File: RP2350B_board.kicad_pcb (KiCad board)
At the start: 2 copper layers, 47.5 x 66 mm, 45 parts, among them IC1 W25Q128JVSIM, IC2 UA78M33CDCYG3, J1 USB_C_Receptacle_USB2.0_16P, J2 SWD, J3 Conn_01x25_Pin, J4 Conn_01x25_Pin, J5 Conn_01x25_Pin, J6 Conn_01x25_Pin, J7 Conn_01x25_Pin, J8 Conn_01x25_Pin, U1 RP2350_80QFN, Y1 ABM8-272-T3

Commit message: refactor: start new layout
Signed-off-by: Aditya Agarwal <aditya.agarwal030504@gmail.com>
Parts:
- removed G***: LOGO, Dumblebots-Logo:Dumblebots-Logo
- removed IC2: UA78M33CDCYG3, UA78M33CDCYG3:SOT230P700X180-4N
- removed R5: 0, Resistor_SMD:R_0402_1005Metric
- removed R8: 1K, Resistor_SMD:R_0402_1005Metric
- added R10: 27, Resistor_SMD:R_0402_1005Metric, F.Cu at (237.2, 104.0)
- added R11: 27, Resistor_SMD:R_0402_1005Metric, F.Cu at (236.2, 104.0)
- added U2: NCP1117-3.3_SOT223, Package_TO_SOT_SMD:SOT-223-3_TabPin2, F.Cu at (242.6, 90.8)
- C19, C20: value 100n -> 10u
- J2: value SWD -> MEM2080-00-128-00-A; footprint Connector_PinHeader_2.54mm:PinHeader_1x04_P2.54mm_Vertical -> MEM2080-00-128-00-A:MEM20800012800A
- L1: footprint Inductor_SMD:L_0603_1608Metric -> Inductor_SMD:L_0805_2012Metric
- R4: value 10K -> 1K
- R6: value DNF -> 10K
- moved R4 122.1 mm to (243.3, 143.4), turned to -90 degrees
- moved C13 108.2 mm to (243.3, 114.0), turned to 0 degrees
- moved C12 104.4 mm to (243.3, 117.7), turned to 0 degrees
- moved C14 104.1 mm to (234.8, 121.8), turned to -90 degrees
- moved C6 102.1 mm to (239.5, 106.2), turned to 0 degrees
- moved C16 99.8 mm to (232.3, 120.9), turned to 180 degrees
- moved C11 99.0 mm to (239.5, 107.2), turned to 0 degrees
- moved R6 97.5 mm to (227.7, 104.7), turned to -45 degrees
- moved C3 95.2 mm to (241.8, 108.4), turned to -90 degrees
- moved S2 95.1 mm to (230.0, 89.7), turned to 90 degrees
- moved C18 94.7 mm to (238.3, 126.5), turned to -90 degrees
- moved R9 94.4 mm to (228.5, 103.9), turned to -45 degrees
- moved C15 92.6 mm to (227.0, 110.7), turned to 180 degrees
- moved R7 92.3 mm to (237.3, 126.5)
- moved L1 92.1 mm to (239.6, 104.6)
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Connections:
- net /VREG_LX renamed VREG_LX
- net Net-(U1-XOUT) renamed XOUT
- C1 pad 1: /VREG_AVDD -> IOVDD
- C1 pad 2: GND -> VREG_PGND
- C10 pad 1: +3.3v -> IOVDD
- C10 pad 2: GND -> VREG_PGND
- C11 pad 1: +3.3v -> IOVDD
- C11 pad 2: GND -> VREG_PGND
- C12 pad 1: +3.3v -> IOVDD
- C12 pad 2: GND -> VREG_PGND
- C13 pad 1: +3.3v -> IOVDD
- C13 pad 2: GND -> VREG_PGND
- C14 pad 1: +3.3v -> IOVDD
- C14 pad 2: GND -> VREG_PGND
- C15 pad 1: +3.3v -> IOVDD
- C15 pad 2: GND -> VREG_PGND
- C16 pad 1: +3.3v -> IOVDD
- C16 pad 2: GND -> VREG_PGND
- C17 pad 1: Net-(U1-XIN) -> VREG_PGND
- C17 pad 2: GND -> XIN
- C18 pad 1: Net-(Y1-CRYSTAL_2) -> VREG_PGND
- C18 pad 2: GND -> Net-(C18-Pad2)
- C19 pad 2: GND -> VREG_PGND
- C2 pad 1: +3.3v -> DVDD
- C2 pad 2: GND -> VREG_PGND
- C20 pad 1: GND -> IOVDD
- C20 pad 2: +3.3v -> VREG_PGND
- C3 pad 1: +1V1 -> VREG_AVDD
- C3 pad 2: GND -> VREG_PGND
- C4 pad 1: +1V1 -> DVDD
- C4 pad 2: GND -> VREG_PGND
- C5 pad 1: +1V1 -> DVDD
- C5 pad 2: GND -> VREG_PGND
- C6 pad 1: +1V1 -> DVDD
- C6 pad 2: GND -> VREG_PGND
- C7 pad 1: +3.3v -> IOVDD
- C7 pad 2: GND -> VREG_PGND
- C8 pad 1: +3.3v -> IOVDD
- C8 pad 2: GND -> VREG_PGND
- C9 pad 1: +3.3v -> IOVDD
- C9 pad 2: GND -> VREG_PGND
- IC1 pad 1: Net-(IC1-~{CS}) -> GPIO0
- IC1 pad 4: GND -> VREG_PGND
- IC1 pad 8: +3.3v -> IOVDD
- J1 pad A1: GND -> VREG_PGND
- J1 pad A12: GND -> VREG_PGND
- J1 pad A6: USB_D+ -> Net-(J1-D+-PadA6)
- J1 pad A7: USB_D- -> Net-(J1-D--PadA7)
- J1 pad B1: GND -> VREG_PGND
- J1 pad B12: GND -> VREG_PGND
- J1 pad B6: USB_D+ -> Net-(J1-D+-PadA6)
- J1 pad B7: USB_D- -> Net-(J1-D--PadA7)
- J1 pad S1: GND -> VREG_PGND
- J2 pad 1: +3.3v -> unconnected-(J2-DAT2-Pad1)
- J2 pad 2: SWD -> unconnected-(J2-CD/DAT3-Pad2)
- J2 pad 3: SWCLK -> unconnected-(J2-CMD-Pad3)
- J2 pad 4: GND -> unconnected-(J2-VDD-Pad4)
- J4 pad 10: GND -> VREG_PGND
- J5 pad 1: GND -> VREG_PGND
- J5 pad 10: GND -> VREG_PGND
- J5 pad 11: GND -> VREG_PGND
- J5 pad 12: GND -> VREG_PGND
- J5 pad 13: GND -> VREG_PGND
- J5 pad 14: GND -> VREG_PGND
- J5 pad 15: GND -> VREG_PGND
- J5 pad 16: GND -> VREG_PGND
- J5 pad 17: GND -> VREG_PGND
- J5 pad 18: GND -> VREG_PGND
- J5 pad 19: GND -> VREG_PGND
- J5 pad 2: GND -> VREG_PGND
- J5 pad 20: GND -> VREG_PGND
- J5 pad 21: GND -> VREG_PGND
- J5 pad 22: GND -> VREG_PGND
- J5 pad 23: GND -> VREG_PGND
- J5 pad 24: GND -> VREG_PGND
- J5 pad 25: GND -> VREG_PGND
- J5 pad 3: GND -> VREG_PGND
- J5 pad 4: GND -> VREG_PGND
- J5 pad 5: GND -> VREG_PGND
- J5 pad 6: GND -> VREG_PGND
- J5 pad 7: GND -> VREG_PGND
- J5 pad 8: GND -> VREG_PGND
- J5 pad 9: GND -> VREG_PGND
- J6 pad 1: GND -> VREG_PGND
- J6 pad 10: GND -> VREG_PGND
- J6 pad 11: GND -> VREG_PGND
- J6 pad 12: GND -> VREG_PGND
- J6 pad 13: GND -> VREG_PGND
- J6 pad 14: GND -> VREG_PGND
- J6 pad 15: GND -> VREG_PGND
- J6 pad 16: GND -> VREG_PGND
- J6 pad 17: GND -> VREG_PGND
- J6 pad 18: GND -> VREG_PGND
- J6 pad 19: GND -> VREG_PGND
- J6 pad 2: GND -> VREG_PGND
- J6 pad 20: GND -> VREG_PGND
- J6 pad 21: GND -> VREG_PGND
- J6 pad 22: GND -> VREG_PGND
- J6 pad 23: GND -> VREG_PGND
- J6 pad 24: GND -> VREG_PGND
- J6 pad 25: GND -> VREG_PGND
- J6 pad 3: GND -> VREG_PGND
- J6 pad 4: GND -> VREG_PGND
- J6 pad 5: GND -> VREG_PGND
- J6 pad 6: GND -> VREG_PGND
- J6 pad 7: GND -> VREG_PGND
- J6 pad 8: GND -> VREG_PGND
- J6 pad 9: GND -> VREG_PGND
- J7 pad 1: +3.3v -> IOVDD
- J7 pad 10: +3.3v -> IOVDD
- J7 pad 11: +3.3v -> IOVDD
- J7 pad 12: +3.3v -> IOVDD
- J7 pad 13: +3.3v -> IOVDD
- J7 pad 14: +3.3v -> IOVDD
- J7 pad 15: +3.3v -> IOVDD
- J7 pad 16: +3.3v -> IOVDD
- J7 pad 17: +3.3v -> IOVDD
- J7 pad 18: +3.3v -> IOVDD
- J7 pad 19: +3.3v -> IOVDD
- J7 pad 2: +3.3v -> IOVDD
- J7 pad 20: +3.3v -> IOVDD
- J7 pad 21: +3.3v -> IOVDD
- J7 pad 22: +3.3v -> IOVDD
- J7 pad 23: +3.3v -> IOVDD
- J7 pad 24: +3.3v -> IOVDD
- J7 pad 25: +3.3v -> IOVDD
- J7 pad 3: +3.3v -> IOVDD
- J7 pad 4: +3.3v -> IOVDD
- J7 pad 5: +3.3v -> IOVDD
- J7 pad 6: +3.3v -> IOVDD
- J7 pad 7: +3.3v -> IOVDD
- J7 pad 8: +3.3v -> IOVDD
- J7 pad 9: +3.3v -> IOVDD
- J8 pad 1: +3.3v -> IOVDD
- J8 pad 10: +3.3v -> IOVDD
- J8 pad 11: +3.3v -> IOVDD
- J8 pad 12: +3.3v -> IOVDD
- J8 pad 13: +3.3v -> IOVDD
- J8 pad 14: +3.3v -> IOVDD
- J8 pad 15: +3.3v -> IOVDD
- J8 pad 16: +3.3v -> IOVDD
- J8 pad 17: +3.3v -> IOVDD
- J8 pad 18: +3.3v -> IOVDD
- J8 pad 19: +3.3v -> IOVDD
- J8 pad 2: +3.3v -> IOVDD
- J8 pad 20: +3.3v -> IOVDD
- J8 pad 21: +3.3v -> IOVDD
- J8 pad 22: +3.3v -> IOVDD
- J8 pad 23: +3.3v -> IOVDD
- J8 pad 24: +3.3v -> IOVDD
- J8 pad 25: +3.3v -> IOVDD
- J8 pad 3: +3.3v -> IOVDD
- J8 pad 4: +3.3v -> IOVDD
- J8 pad 5: +3.3v -> IOVDD
- J8 pad 6: +3.3v -> IOVDD
- J8 pad 7: +3.3v -> IOVDD
- J8 pad 8: +3.3v -> IOVDD
- J8 pad 9: +3.3v -> IOVDD
- L1 pad 1: +1V1 -> DVDD
- R1 pad 1: +3.3v -> IOVDD
- R1 pad 2: /VREG_AVDD -> VREG_AVDD
- R2 pad 2: GND -> VREG_PGND
- R3 pad 2: GND -> VREG_PGND
- R4 pad 1: Net-(IC1-~{CS}) -> VREG_PGND
- R4 pad 2: +3.3v -> Net-(S1-NO)
- R6 pad 2: Net-(IC1-~{CS}) -> IOVDD
- R7 pad 1: Net-(Y1-CRYSTAL_2) -> Net-(C18-Pad2)
- R9 pad 1: GND -> GPIO0
- R9 pad 2: Net-(S2-NO) -> Net-(S2-COM)
- S2 pad 1: QSPI_SS -> Net-(S2-COM)
- S2 pad 2: Net-(S2-NO) -> VREG_PGND
- U1 pad 10: +1V1 -> DVDD
- U1 pad 15: +3.3v -> IOVDD
- U1 pad 24: +3.3v -> IOVDD
- U1 pad 29: +3.3v -> IOVDD
- U1 pad 30: Net-(U1-XIN) -> XIN
- U1 pad 32: +1V1 -> DVDD
- U1 pad 41: +3.3v -> IOVDD
- U1 pad 5: +3.3v -> IOVDD
- U1 pad 50: +3.3v -> IOVDD
- U1 pad 51: +1V1 -> DVDD
- U1 pad 59: +3.3v -> IOVDD
- U1 pad 60: +3.3v -> IOVDD
- U1 pad 61: /VREG_AVDD -> VREG_AVDD
- U1 pad 62: GND -> VREG_PGND
- U1 pad 64: +3.3v -> IOVDD
- U1 pad 65: +1V1 -> DVDD
- U1 pad 68: +3.3v -> IOVDD
- U1 pad 69: +3.3v -> IOVDD
- U1 pad 75: QSPI_SS -> GPIO0
- U1 pad 76: +3.3v -> IOVDD
- U1 pad 81: GND -> VREG_PGND
- Y1 pad 1: Net-(U1-XIN) -> XIN
- Y1 pad 2: GND -> VREG_PGND
- Y1 pad 3: Net-(Y1-CRYSTAL_2) -> Net-(C18-Pad2)
- Y1 pad 4: GND -> VREG_PGND
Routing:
- net +3.3v: track 421.7 -> 0.00 mm, vias 16 -> 0
- net QSPI_SS: track 50.9 -> 0.00 mm, vias 1 -> 0
- net IOVDD: track 0.00 -> 48.8 mm, vias 0 -> 2
- net GND: track 37.4 -> 0.00 mm, vias 27 -> 0
- net GPIO47: track 33.0 -> 0.00 mm
- net GPIO25: track 32.1 -> 0.00 mm, vias 2 -> 0
- net GPIO46: track 31.9 -> 0.00 mm
- net GPIO45: track 30.8 -> 0.00 mm
- net GPIO1: track 30.5 -> 0.00 mm
- net GPIO26: track 30.3 -> 0.00 mm, vias 2 -> 0
- net GPIO24: track 29.5 -> 0.00 mm
- net GPIO2: track 27.8 -> 0.00 mm
- net GPIO27: track 26.8 -> 0.00 mm, vias 2 -> 0
- net GPIO23: track 26.6 -> 0.00 mm
- net GPIO44: track 25.6 -> 0.00 mm
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- removed copper zone on B.Cu, net GND
- removed copper zone on F.Cu, net GND
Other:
- board size 47.5 x 66 mm -> 43 x 79 mm
- board text removed: "05"
- board text removed: "06"
- board text removed: "12"
- board text removed: "3V3"
- board text removed: "42"
- board text removed: "43"
- board text removed: "44"
- board text removed: "BOOT"
- board text removed: "Designed and manufactured in Bharat"
- board text removed: "GND"
- board text removed: "GPIO01"
- board text removed: "GPIO02"
- board text removed: "GPIO03"
- board text removed: "GPIO04"
- board text removed: "GPIO07"
- board text removed: "GPIO08"
- board text removed: "GPIO09"
- board text removed: "GPIO10"
- board text removed: "GPIO11"
- board text removed: "GPIO13"
- board text removed: "GPIO14"
- board text removed: "GPIO15"
- board text removed: "GPIO16"
- board text removed: "GPIO17"
- board text removed: "GPIO18"
- board text removed: "GPIO19"
- board text removed: "GPIO20"
- board text removed: "GPIO21"
- board text removed: "GPIO22"
- board text removed: "GPIO23"
- board text removed: "GPIO24"
- board text removed: "GPIO25"
- board text removed: "GPIO26"
- board text removed: "GPIO27"
- board text removed: "GPIO28"
- board text removed: "GPIO29"
- board text removed: "GPIO30"
- board text removed: "GPIO31"
- board text removed: "GPIO32"
- board text removed: "GPIO33"
- board text removed: "GPIO34"
- board text removed: "GPIO35"
- board text removed: "GPIO36"
- board text removed: "GPIO37"
- board text removed: "GPIO38"
- board text removed: "GPIO39"
- board text removed: "GPIO40"
- board text removed: "GPIO41"
- board text removed: "GPIO45"
- board text removed: "GPIO46"
- board text removed: "GPIO47"
- board text removed: "RP2350B Dev Board"
- board text removed: "RST"
- board text removed: "SWCLK"
- board text removed: "SWDIO"
- board text removed: "VUSB"
- board text removed: "dumblebots.com"

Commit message: feat: complete all features except SD Card reader
Signed-off-by: Aditya Agarwal <aditya.agarwal030504@gmail.com>
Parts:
- added REF**: MountingHole_2.2mm_M2_Pad, MountingHole:MountingHole_2.2mm_M2_Pad, F.Cu at (153.8, 135.3)
- added REF**: MountingHole_2.2mm_M2_Pad, MountingHole:MountingHole_2.2mm_M2_Pad, F.Cu at (114.8, 135.3)
- added REF**: MountingHole_2.2mm_M2_Pad, MountingHole:MountingHole_2.2mm_M2_Pad, F.Cu at (153.8, 61.4)
- added REF**: MountingHole_2.2mm_M2_Pad, MountingHole:MountingHole_2.2mm_M2_Pad, F.Cu at (114.8, 61.4)
- moved C12 103.1 mm to (140.6, 108.6), turned to -90 degrees
- moved C2 102.6 mm to (125.0, 102.4), turned to 135 degrees
- moved R4 102.5 mm to (142.1, 127.4), turned to 90 degrees
- moved C16 102.1 mm to (130.8, 110.3), turned to -135 degrees
- moved J1 102.0 mm to (134.3, 62.6)
- moved C10 101.9 mm to (141.6, 98.4)
- moved R2 101.9 mm to (135.8, 68.8)
- moved R3 101.9 mm to (133.0, 68.9)
- moved C1 101.8 mm to (125.8, 105.4)
- moved IC1 101.7 mm to (128.6, 86.9)
- moved L1 101.7 mm to (138.3, 94.2)
- moved Y1 101.7 mm to (132.6, 115.8)
- moved R9 101.7 mm to (127.3, 93.5)
- moved C11 101.7 mm to (138.3, 96.8)
- moved C18 101.7 mm to (137.1, 116.1)
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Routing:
- net IOVDD: track 48.8 -> 200.8 mm
- net GPIO47: track 0.00 -> 36.9 mm, vias 0 -> 1
- net GPIO25: track 0.00 -> 35.6 mm
- net GPIO1: track 0.00 -> 35.3 mm, vias 0 -> 1
- net GPIO46: track 0.00 -> 34.8 mm, vias 0 -> 1
- net GPIO26: track 0.00 -> 34.2 mm
- net GPIO2: track 0.00 -> 33.0 mm, vias 0 -> 1
- net VBUS: track 28.1 -> 61.0 mm
- net GPIO45: track 0.00 -> 32.8 mm, vias 0 -> 1
- net GPIO27: track 0.00 -> 32.7 mm
- net GPIO44: track 0.00 -> 31.1 mm, vias 0 -> 1
- net GPIO3: track 0.00 -> 30.6 mm, vias 0 -> 1
- net GPIO43: track 0.00 -> 28.7 mm, vias 0 -> 1
- net GPIO4: track 0.00 -> 27.8 mm
- net GPIO42: track 0.00 -> 26.7 mm
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- added copper zone on B.Cu, net VREG_PGND
- added copper zone on F.Cu, net VREG_PGND
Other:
- board size 43 x 79 mm -> 43.9 x 79 mm

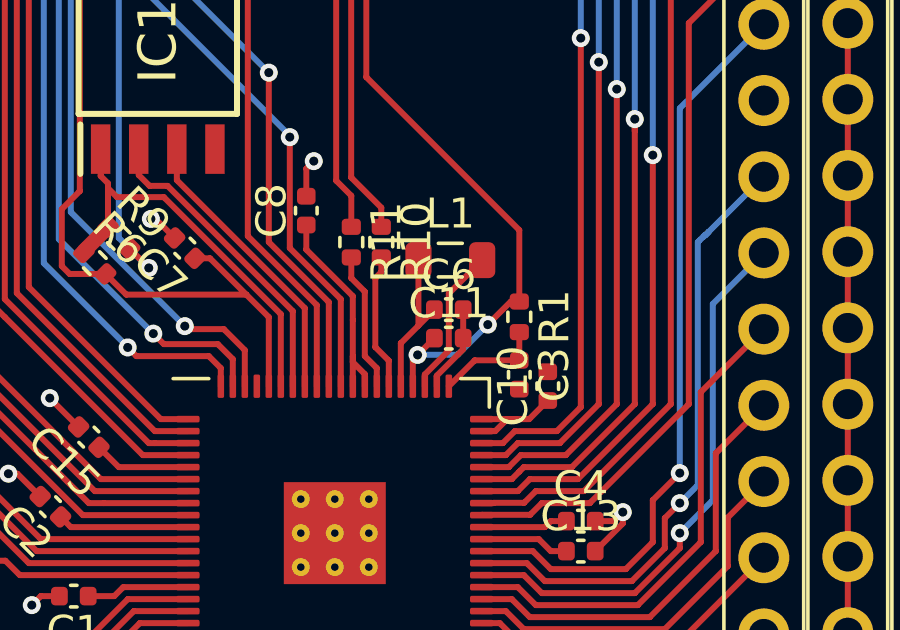
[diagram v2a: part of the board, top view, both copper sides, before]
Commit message: fix: remove copper area from under inductor
Signed-off-by: Aditya Agarwal <aditya.agarwal030504@gmail.com>
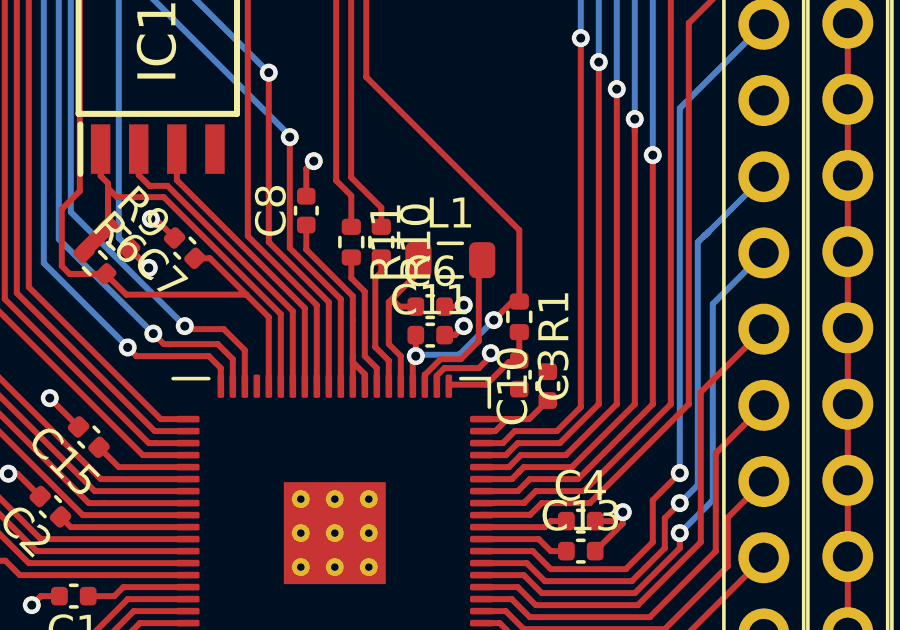
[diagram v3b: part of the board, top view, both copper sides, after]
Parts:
- moved C11 0.63 mm to (137.7, 96.7)
- moved C6 0.63 mm to (137.7, 95.8)
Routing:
- net VREG_PGND: track 25.3 -> 26.3 mm, vias 15 -> 18
- net DVDD: track 15.3 -> 15.9 mm

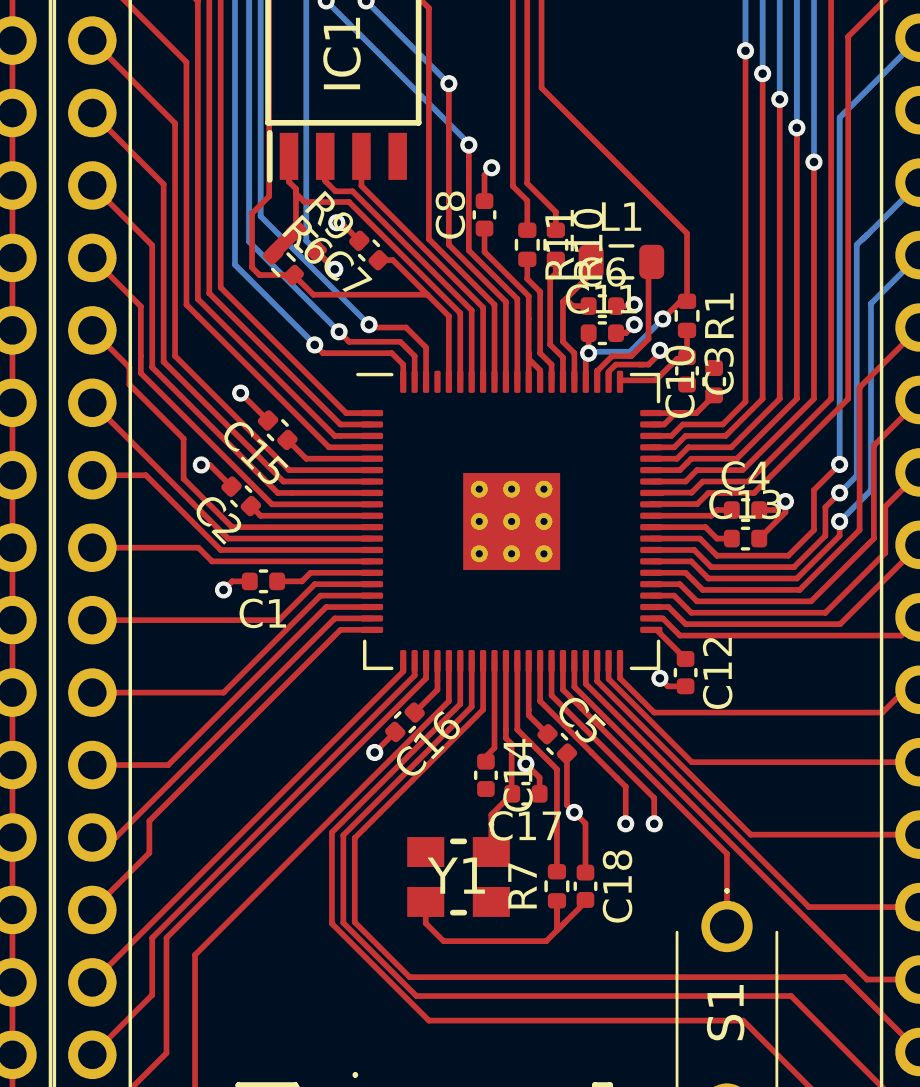
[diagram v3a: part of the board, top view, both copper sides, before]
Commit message: fix: add seperate via for Cfilter
Signed-off-by: Aditya Agarwal <aditya.agarwal030504@gmail.com>
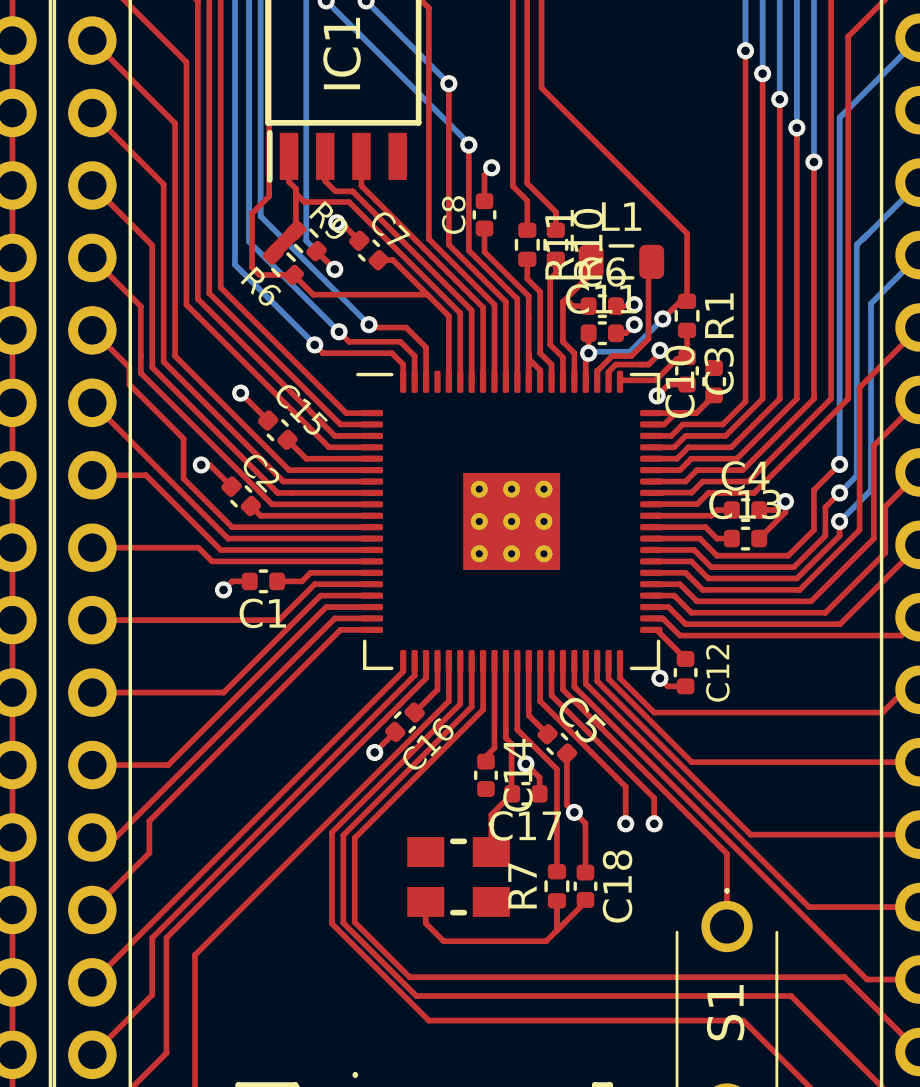
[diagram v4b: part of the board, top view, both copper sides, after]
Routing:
- net VREG_PGND: track 26.3 -> 27.5 mm, vias 18 -> 19
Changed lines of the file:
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@@
 		(tags "capacitor")
 		(property "Reference" "C2"
-			(at 0 -1.16 135)
+			(at 0.098578 1.06066 135)
 			(layer "F.SilkS")
 			(effects
 				(font
-					(size 1 1)
+					(size 0.8 0.8)
 					(thickness 0.15)
 				)
@@
 			(at 0 0 0)
 			(layer "F.SilkS")
+			(hide yes)
 			(effects
 				(font
@@
 			(effects
 				(font
-					(size 1 1)
+					(size 0.8 0.8)
 					(thickness 0.15)
 				)
@@
 		(tags "resistor")
 		(property "Reference" "R6"
-			(at 0 -1.17 135)
+			(at 0 1.131371 135)
 			(layer "F.SilkS")
 			(effects
 				(font
-					(size 1 1)
+					(size 0.8 0.8)
 					(thickness 0.15)
 				)
@@
 		(tags "capacitor")
 		(property "Reference" "C7"
-			(at 0 -1.16 135)
+			(at 0 0.989949 135)
 			(layer "F.SilkS")
 			(effects
 				(font
-					(size 1 1)
+					(size 0.8 0.8)
 					(thickness 0.15)
 				)
@@
 		(tags "resistor")
 		(property "Reference" "R9"
-			(at 0 -1.17 135)
+			(at 0.098554 -1.032817 135)
 			(layer "F.SilkS")
 			(effects
 				(font
-					(size 1 1)
+					(size 0.8 0.8)
 					(thickness 0.15)
 				)
@@
 		(tags "capacitor")
 		(property "Reference" "C15"
-			(at 0 -1.16 135)
+			(at -0.070711 1.06066 135)
 			(layer "F.SilkS")
 			(effects
 				(font
-					(size 1 1)
+					(size 0.8 0.8)
 					(thickness 0.15)
 				)
@@
 		(tags "capacitor")
 		(property "Reference" "C8"
-			(at 0 -1.16 90)
+			(at 0 -1.05 90)
 			(layer "F.SilkS")
 			(effects
 				(font
-					(size 1 1)
+					(size 0.8 0.8)
 					(thickness 0.15)
 				)
@@
 			(effects
 				(font
-					(size 1 1)
+					(size 0.8 0.8)
 					(thickness 0.15)
 				)
@@
 	)
 	(segment
+		(start 140.65 98.5)
+		(end 140 98.5)
+		(width 0.2)
+		(layer "F.Cu")
+		(net 1)
+	)
+	(segment
 		(start 133.55 92.07)
 		(end 133.55 91.15)
@@
 	)
 	(segment
+		(start 140 98.5)
+		(end 139.6 98.9)
+		(width 0.2)
+		(layer "F.Cu")
+		(net 1)
+	)
+	(segment
 		(start 138.16 95.75)
 		(end 138.75 95.75)
@@
 		(size 0.6)
 		(drill 0.3)
+		(layers "F.Cu" "B.Cu")
+		(net 1)
+	)
+	(via
+		(at 139.6 98.9)
+		(size 0.6)
+		(drill 0.3)
